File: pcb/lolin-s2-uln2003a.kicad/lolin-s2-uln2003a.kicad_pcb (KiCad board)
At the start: 2 copper layers, 65.3 x 42.3 mm, 19 parts, among them J1 Conn_S2_Left, J10 Micro_SD_TF_PUSH, J11 Vin Barrel-Jack, J12 Conn_LED2, J2 Conn_S2_Right, J3 Conn_PWR, J4 Conn_Motor, J5 Conn_LED1, J6 Conn_LED3, J7 Conn_I2S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

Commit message: fixed rotation of motor-connector
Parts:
- moved J4 10.1 mm to (136.6, 90.0), turned to 90 degrees
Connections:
- J4 pad 1: VCC -> /Blue
- J4 pad 2: /Orange -> /Purple
- J4 pad 4: /Purple -> /Orange
- J4 pad 5: /Blue -> VCC
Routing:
- net /Orange: track 10.7 -> 9.34 mm
- net /Yellow: track 10.2 -> 9.18 mm
- net /Purple: track 9.72 -> 8.67 mm
- net /Blue: track 9.22 -> 8.17 mm
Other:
- board text added: "Rev. 1.01"
- board text removed: "Rev. 1.00"
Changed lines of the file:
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@@
   )
   (footprint "Connector_JST:JST_XH_B5B-XH-A_1x05_P2.50mm_Vertical" (layer "F.Cu")
-    (at 137.6 80 -90)
+    (at 136.55 90 90)
     (descr "JST XH series connector, B5B-XH-A (http://www.jst-mfg.com/product/pdf/eng/eXH.pdf), generated with kicad-footprint-generator")
     (tags "connector JST XH vertical")
@@
     (fp_line (start 12.45 3.4) (end 12.45 -2.35)
       (stroke (width 0.1) (type solid)) (layer "F.Fab"))
-    (pad "1" thru_hole roundrect (at 0 0 270) (size 1.7 1.95) (drill 0.95) (layers "*.Cu" "*.Mask") (roundrect_rratio 0.1470588235)
-      (net 32 "VCC") (pinfunction "Pin_1") (pintype "passive"))
-    (pad "2" thru_hole oval (at 2.5 0 270) (size 1.7 1.95) (drill 0.95) (layers "*.Cu" "*.Mask")
-      (net 33 "/Orange") (pinfunction "Pin_2") (pintype "passive"))
-    (pad "3" thru_hole oval (at 5 0 270) (size 1.7 1.95) (drill 0.95) (layers "*.Cu" "*.Mask")
+    (pad "1" thru_hole roundrect (at 0 0 90) (size 1.7 1.95) (drill 0.95) (layers "*.Cu" "*.Mask") (roundrect_rratio 0.1470588235)
+      (net 36 "/Blue") (pinfunction "Pin_1") (pintype "passive"))
+    (pad "2" thru_hole oval (at 2.5 0 90) (size 1.7 1.95) (drill 0.95) (layers "*.Cu" "*.Mask")
+      (net 35 "/Purple") (pinfunction "Pin_2") (pintype "passive"))
+    (pad "3" thru_hole oval (at 5 0 90) (size 1.7 1.95) (drill 0.95) (layers "*.Cu" "*.Mask")
       (net 34 "/Yellow") (pinfunction "Pin_3") (pintype "passive"))
-    (pad "4" thru_hole oval (at 7.5 0 270) (size 1.7 1.95) (drill 0.95) (layers "*.Cu" "*.Mask")
-      (net 35 "/Purple") (pinfunction "Pin_4") (pintype "passive"))
-    (pad "5" thru_hole oval (at 10 0 270) (size 1.7 1.95) (drill 0.95) (layers "*.Cu" "*.Mask")
-      (net 36 "/Blue") (pinfunction "Pin_5") (pintype "passive"))
+    (pad "4" thru_hole oval (at 7.5 0 90) (size 1.7 1.95) (drill 0.95) (layers "*.Cu" "*.Mask")
+      (net 33 "/Orange") (pinfunction "Pin_4") (pintype "passive"))
+    (pad "5" thru_hole oval (at 10 0 90) (size 1.7 1.95) (drill 0.95) (layers "*.Cu" "*.Mask")
+      (net 32 "VCC") (pinfunction "Pin_5") (pintype "passive"))
     (model "${KICAD6_3DMODEL_DIR}/Connector_JST.3dshapes/JST_XH_B5B-XH-A_1x05_P2.50mm_Vertical.wrl"
       (offset (xyz 0 0 0))
@@
     (effects (font (size 1 1) (thickness 0.1)) (justify right bottom mirror))
   )
-  (gr_text "Rev. 1.00" (at 84 118.1) (layer "B.SilkS")
+  (gr_text "Rev. 1.01" (at 84 118.1) (layer "B.SilkS")
     (effects (font (size 1 1) (thickness 0.1)) (justify left bottom mirror))
   )
@@
   (segment (start 92.38 98.1) (end 87.18 92.9) (width 0.4) (layer "B.Cu") (net 31))
   (segment (start 123.8 103.24) (end 126.14 100.9) (width 0.4) (layer "B.Cu") (net 31))
-  (segment (start 136.2 82.5) (end 137.6 82.5) (width 0.2) (layer "F.Cu") (net 33))
   (segment (start 130.32 88.38) (end 136.2 82.5) (width 0.2) (layer "F.Cu") (net 33))
   (segment (start 129.3 88.38) (end 130.32 88.38) (width 0.2) (layer "F.Cu") (net 33))
   (segment (start 129.3 89.65) (end 130.35 89.65) (width 0.2) (layer "F.Cu") (net 34))
-  (segment (start 135 85) (end 137.6 85) (width 0.2) (layer "F.Cu") (net 34))
   (segment (start 130.35 89.65) (end 135 85) (width 0.2) (layer "F.Cu") (net 34))
+  (segment (start 135 85) (end 136.55 85) (width 0.2) (layer "F.Cu") (net 34))
+  (segment (start 134.3 87.5) (end 136.55 87.5) (width 0.2) (layer "F.Cu") (net 35))
   (segment (start 129.3 90.92) (end 130.88 90.92) (width 0.2) (layer "F.Cu") (net 35))
   (segment (start 130.88 90.92) (end 134.3 87.5) (width 0.2) (layer "F.Cu") (net 35))
-  (segment (start 134.3 87.5) (end 137.6 87.5) (width 0.2) (layer "F.Cu") (net 35))
   (segment (start 129.3 92.19) (end 131.39 92.19) (width 0.2) (layer "F.Cu") (net 36))
-  (segment (start 133.6 90) (end 137.6 90) (width 0.2) (layer "F.Cu") (net 36))
   (segment (start 131.39 92.19) (end 131.4 92.2) (width 0.2) (layer "F.Cu") (net 36))
+  (segment (start 133.6 90) (end 136.55 90) (width 0.2) (layer "F.Cu") (net 36))
   (segment (start 131.4 92.2) (end 133.6 90) (width 0.2) (layer "F.Cu") (net 36))
   (segment (start 131.46 93.46) (end 136.55 98.55) (width 0.2) (layer "F.Cu") (net 37))

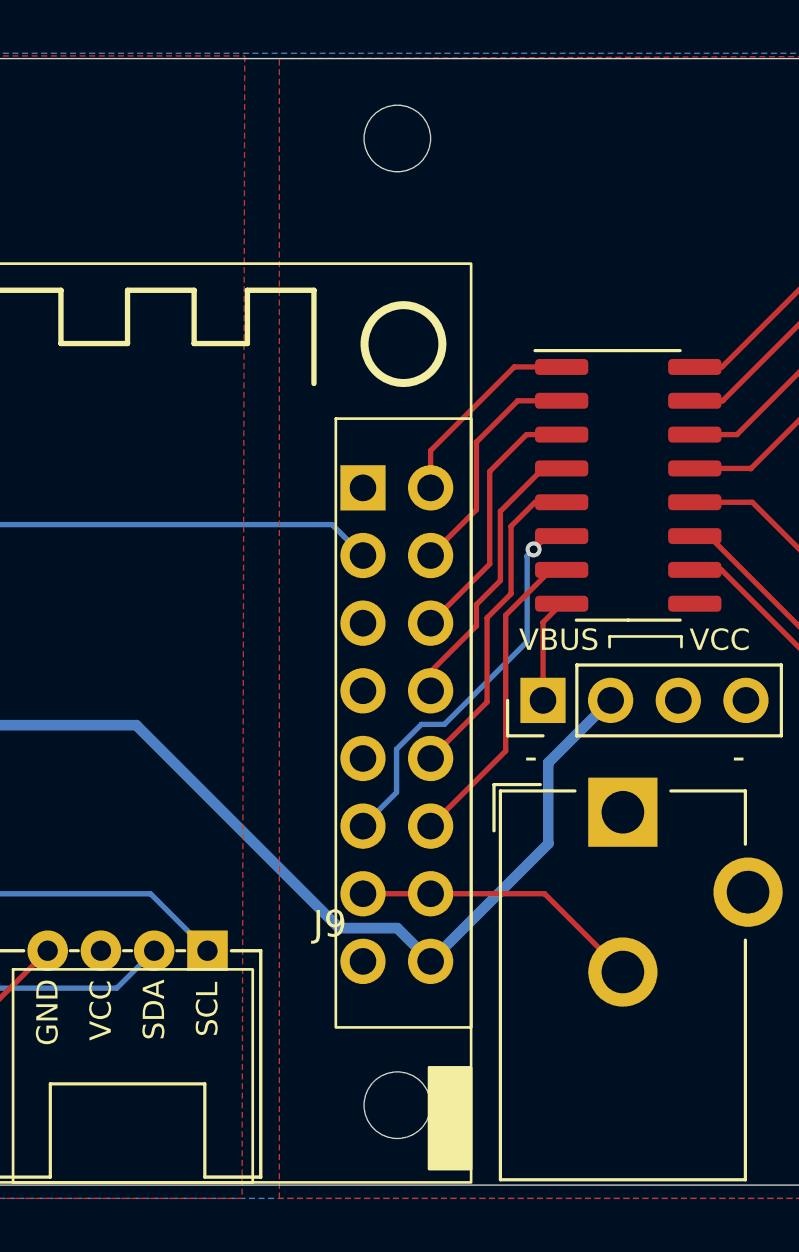
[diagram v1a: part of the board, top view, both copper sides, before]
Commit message: symmetric mounting holes
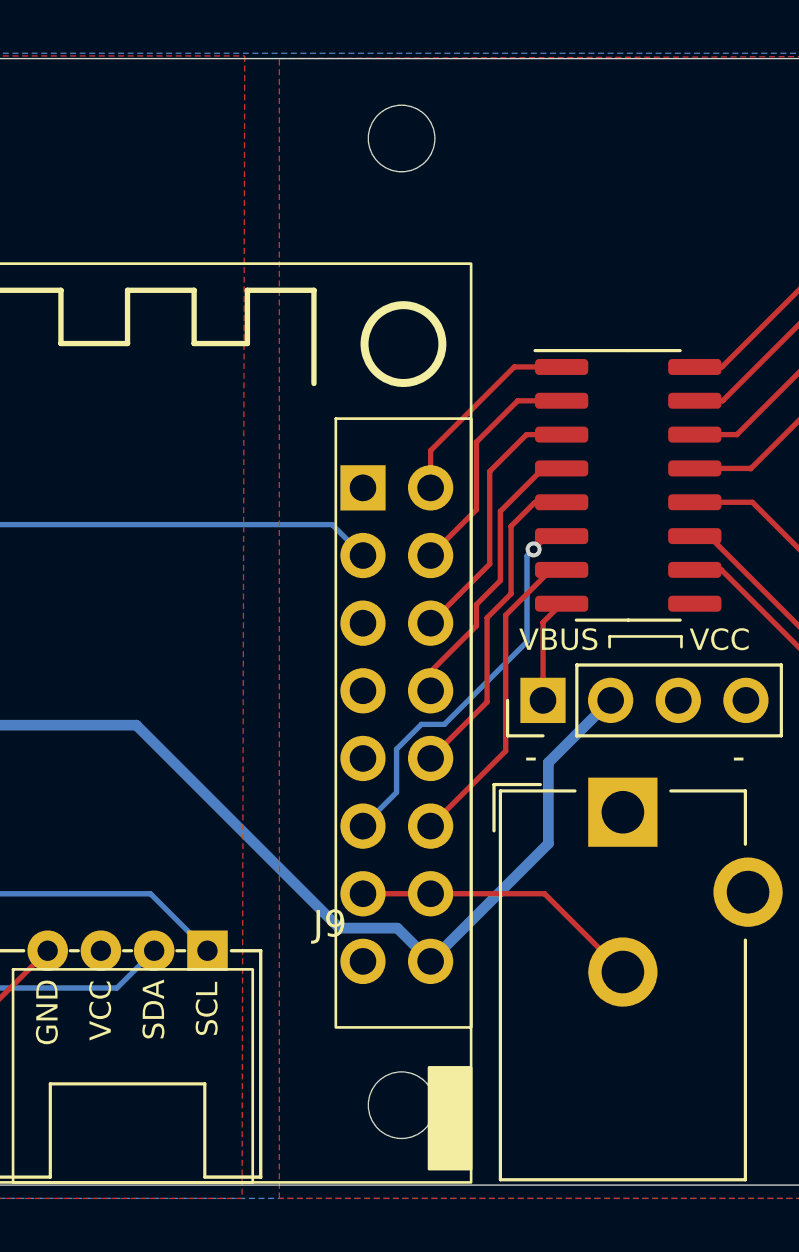
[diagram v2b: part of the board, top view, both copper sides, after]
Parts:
- moved H2 0.16 mm to (118.3, 79.8)
- moved H4 0.16 mm to (118.3, 116.1)
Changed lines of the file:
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@@
   (net 43 "/GPIO38")
   (footprint "MountingHole:MountingHole_2.5mm" (layer "F.Cu")
-    (at 118.13 116.1)
+    (at 118.29 116.1)
     (descr "Mounting Hole 2.5mm, no annular")
     (tags "mounting hole 2.5mm no annular")
@@
   )
   (footprint "MountingHole:MountingHole_2.5mm" (layer "F.Cu")
-    (at 118.13 79.8)
+    (at 118.29 79.8)
     (descr "Mounting Hole 2.5mm, no annular")
     (tags "mounting hole 2.5mm no annular")
